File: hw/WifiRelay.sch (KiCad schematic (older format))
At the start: 35 parts, among them J1 CONN_01X02, J2 CONN_01X06, J3 CONN_01X02, J4 CONN_01X02, J5 TEST_1P, J6 TEST_1P, K1 Songle-SRD-05VDC-SL-C, K2 Songle-SRD-05VDC-SL-C, Q1 MMSS8050-H, Q2 MMSS8050-H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

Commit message: Updated symbol and footprint libraries to use KiCad 5 versions.
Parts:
- removed U3: ESP-07v2, ESP8266:ESP-07v2, symbol ESP8266:ESP-07v2
- added U3: ESP-07, RF_Module:ESP-07, symbol RF_Module:ESP-07
- C1: footprint Capacitors_Tantalum_SMD:CP_Tantalum_Case-A_EIA-3216-18_Reflow -> Capacitor_Tantalum_SMD:CP_EIA-3216-18_Kemet-A; symbol device:CP -> Device:CP
- C2: footprint Capacitors_Tantalum_SMD:CP_Tantalum_Case-B_EIA-3528-21_Reflow -> Capacitor_Tantalum_SMD:CP_EIA-3528-21_Kemet-B; symbol device:CP -> Device:CP
- C3: footprint Capacitors_SMD:C_0805 -> Capacitor_SMD:C_0805_2012Metric; symbol device:C -> Device:C
- C4: symbol device:C -> Device:C
- D1, D2: footprint Diodes_SMD:D_SOD-123 -> Diode_SMD:D_SOD-123; symbol WifiRelay:1N4148 -> Diode:1N4148
- J1, J4: footprint Connectors_Terminal_Blocks:TerminalBlock_Pheonix_MKDS1.5-2pol -> TerminalBlock_Phoenix:TerminalBlock_Phoenix_MKDS-1,5-2_1x02_P5.00mm_Horizontal; symbol conn:CONN_01X02 -> Connector_Generic:Conn_01x02
- J2: footprint Pin_Headers:Pin_Header_Straight_1x06_Pitch2.54mm -> Connector_PinHeader_2.54mm:PinHeader_1x06_P2.54mm_Vertical; symbol conn:CONN_01X06 -> Connector_Generic:Conn_01x06
- J3: symbol conn:CONN_01X02 -> Connector_Generic:Conn_01x02
- J5, J6: footprint Pin_Headers:Pin_Header_Straight_1x01_Pitch2.54mm -> Connector_PinHeader_2.54mm:PinHeader_1x01_P2.54mm_Vertical; symbol conn:TEST_1P -> Connector:TestPoint
- JP1: footprint Pin_Headers:Pin_Header_Straight_1x03_Pitch2.54mm -> Connector_PinHeader_2.54mm:PinHeader_1x03_P2.54mm_Vertical; symbol WifiRelay:Jumper_Dual -> Jumper:Jumper_3_Bridged12
- K1, K2: footprint Relays_THT:Relay_SPDT_SANYOU_SRD_Series_Form_C -> Relay_THT:Relay_SPDT_SANYOU_SRD_Series_Form_C; symbol WifiRelay:Songle-SRD-05VDC-SL-C -> Relay:SANYOU_SRD_Form_C
- Q1, Q2: footprint TO_SOT_Packages_SMD:SOT-23 -> Package_TO_SOT_SMD:SOT-23; symbol transistors:MMSS8050-H -> WifiRelay:MMSS8050-H
- R1, R10, R11, R12, R2, R3, R4, R5, R6, R7, R8, R9: footprint Resistors_SMD:R_0805 -> Resistor_SMD:R_0805_2012Metric; symbol device:R -> Device:R
- SW1, SW2: footprint Buttons_Switches_SMD:SW_SPST_TL3342 -> Button_Switch_SMD:SW_SPST_TL3342; symbol switches:SW_Push -> Switch:SW_Push
- U1: symbol WifiRelay:IRM-02-5 -> Converter_ACDC:IRM-02-5
- U2: footprint TO_SOT_Packages_SMD:SOT-223-3Lead_TabPin2 -> Package_TO_SOT_SMD:SOT-223-3_TabPin2; symbol regul:LM1117-3.3 -> Regulator_Linear:LM1117-3.3
- U4: symbol opto:PC827 -> Isolator:PC827
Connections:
- wire segments 105 -> 114
- no-connect marks 8 -> 9
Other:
- moved on the sheet: R12, R3, R4, SW2, U1

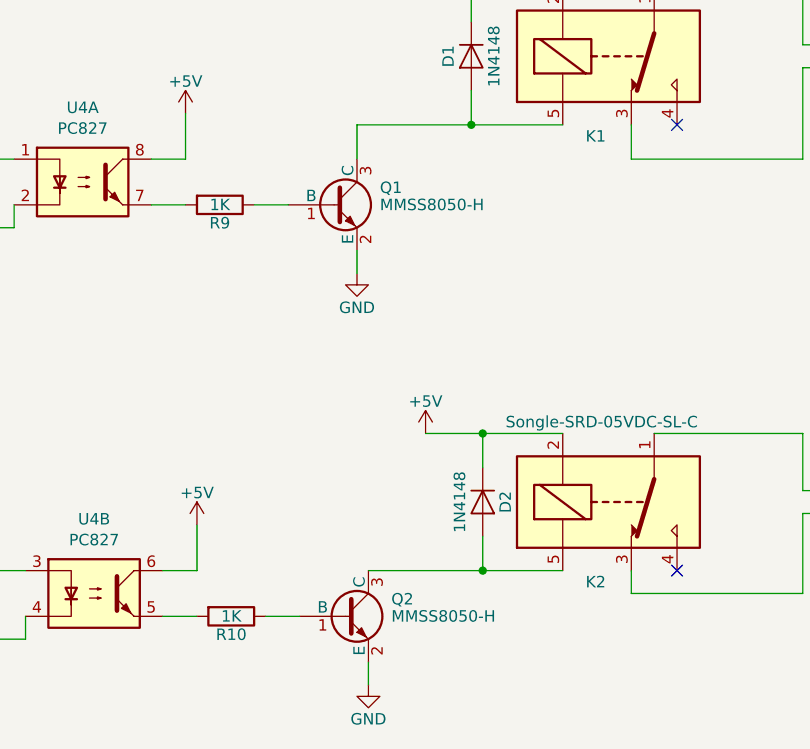
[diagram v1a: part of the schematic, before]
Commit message: Updated symbol for MMSS8050-H transistor to use new KiCad library symbol
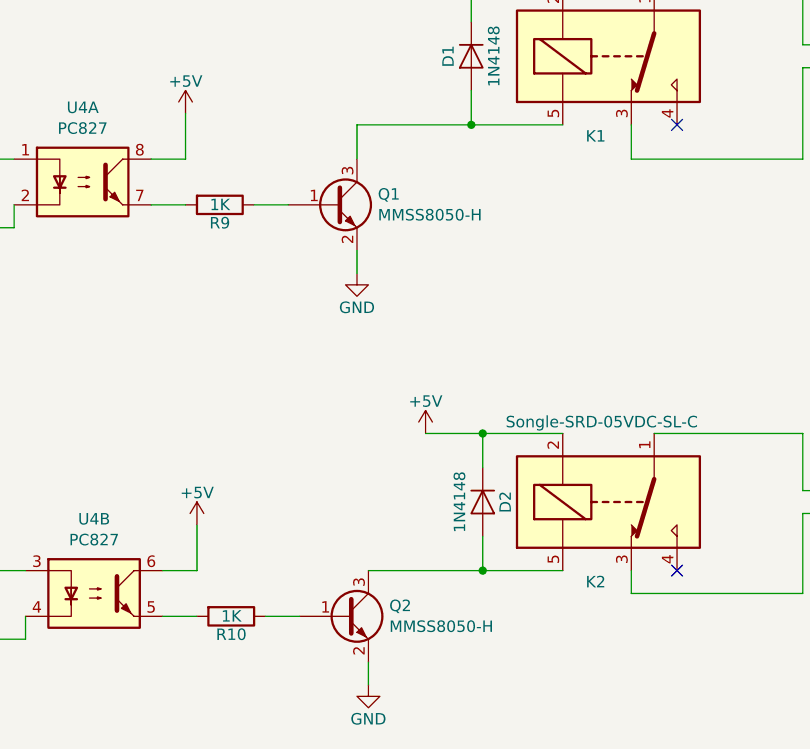
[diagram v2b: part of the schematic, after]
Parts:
- removed Q1, Q2: MMSS8050-H, Package_TO_SOT_SMD:SOT-23, symbol WifiRelay:MMSS8050-H
- added Q1, Q2: MMSS8050-H, Package_TO_SOT_SMD:SOT-23, symbol Device:Q_NPN_BEC
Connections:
- net GND: now also Q1.2 (E), Q2.2 (E)
- net at D2.2 (A), K2.5: now also Q2.3 (C)
- net at R9.1: now also Q1.1 (B)
- net at R10.1: now also Q2.1 (B)
- net at D1.2 (A), K1.5: now also Q1.3 (C)
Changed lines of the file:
@@
-$EndComp
-$Comp
-L WifiRelay:MMSS8050-H Q2
-U 1 1 58F2A851
-P 6450 5900
-F 0 "Q2" H 6650 5975 50  0000 L CNN
-F 1 "MMSS8050-H" H 6650 5900 50  0000 L CNN
-F 2 "Package_TO_SOT_SMD:SOT-23" H 6650 5825 50  0001 L CIN
-F 3 "" H 6450 5900 50  0001 L CNN
-F 4 "MMSS8050-H-TP" H 6450 5900 60  0001 C CNN "MPN"
-F 5 "MMSS8050-H-TPMSCT-ND" H 6450 5900 60  0001 C CNN "DPN"
-	1    6450 5900
-	1    0    0    -1
-$EndComp
-$Comp
-L WifiRelay:MMSS8050-H Q1
-U 1 1 58F2B026
-P 6400 4100
-F 0 "Q1" H 6600 4175 50  0000 L CNN
-F 1 "MMSS8050-H" H 6600 4100 50  0000 L CNN
-F 2 "Package_TO_SOT_SMD:SOT-23" H 6600 4025 50  0001 L CIN
-F 3 "" H 6400 4100 50  0001 L CNN
-F 4 "MMSS8050-H-TP" H 6400 4100 60  0001 C CNN "MPN"
-F 5 "MMSS8050-H-TPMSCT-ND" H 6400 4100 60  0001 C CNN "DPN"
-	1    6400 4100
-	1    0    0    -1
 $EndComp
 $Comp
@@
 Wire Wire Line
 	1950 4600 1950 4800
+$Comp
+L Device:Q_NPN_BEC Q2
+U 1 1 5C3BACBF
+P 6450 5900
+F 0 "Q2" H 6641 5946 50  0000 L CNN
+F 1 "MMSS8050-H" H 6641 5855 50  0000 L CNN
+F 2 "Package_TO_SOT_SMD:SOT-23" H 6650 6000 50  0001 C CNN
+F 3 "" H 6450 5900 50  0001 C CNN
+	1    6450 5900
+	1    0    0    -1
+$EndComp
+$Comp
+L Device:Q_NPN_BEC Q1
+U 1 1 5C3BAF9E
+P 6400 4100
+F 0 "Q1" H 6591 4146 50  0000 L CNN
+F 1 "MMSS8050-H" H 6591 4055 50  0000 L CNN
+F 2 "Package_TO_SOT_SMD:SOT-23" H 6600 4200 50  0001 C CNN
+F 3 "" H 6400 4100 50  0001 C CNN
+	1    6400 4100
+	1    0    0    -1
+$EndComp
 $EndSCHEMATC
